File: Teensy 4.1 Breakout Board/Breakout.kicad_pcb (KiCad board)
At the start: 2 copper layers, 81.4 x 64.3 mm, 59 parts, among them J1 CAN, J10 RTD_Speaker, J11 Current Sensor Power source, J12 RTD_button, J2 12V Power, J3 APPS1, J4 APPS2, J5 Brake_Pressure_Front, J6 Brake_Pressure_Rear, J7 Nextion, J8 ESP32, J9 Brake_Light, Q1 2N7000, Q2 2N7000, U1 SN65HVD230, U3 Teensy4.1, U4 TPS62163DSG, U5 MPU6050

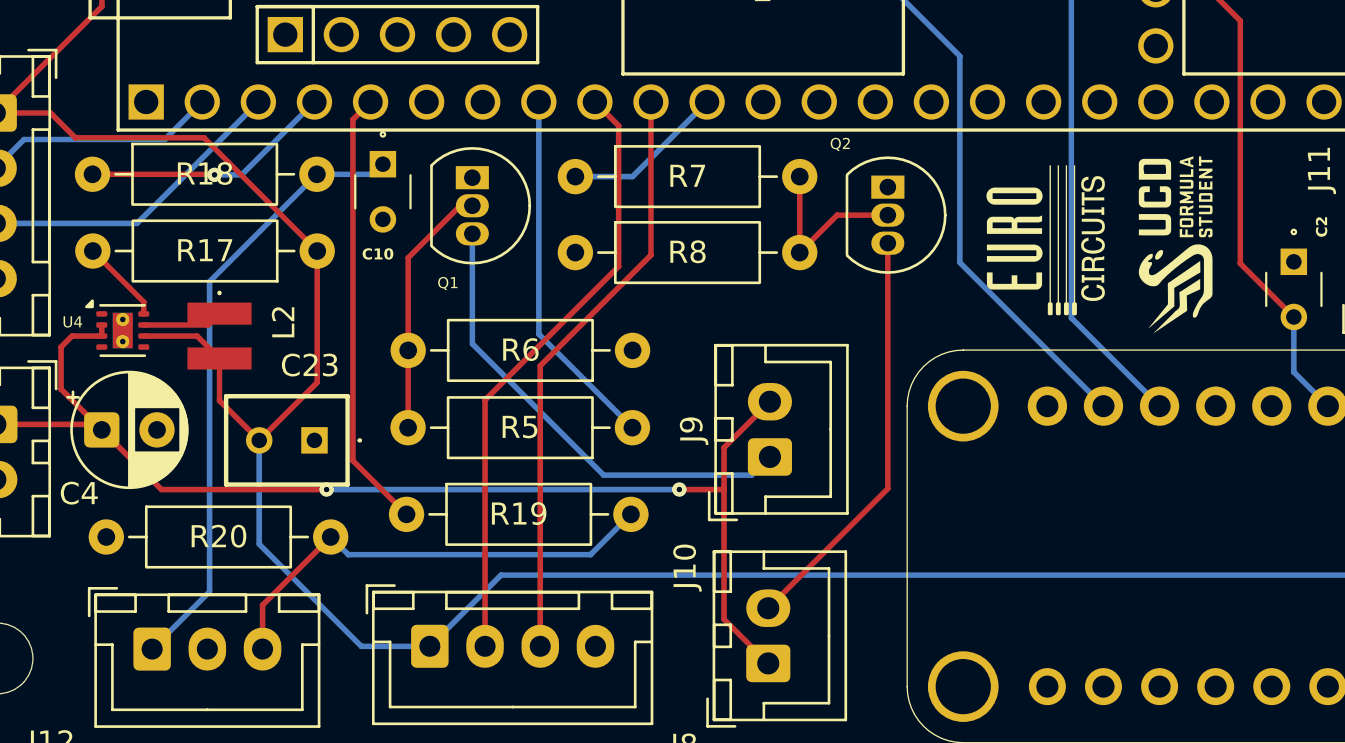
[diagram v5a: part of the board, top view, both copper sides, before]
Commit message: slave with new fuses added
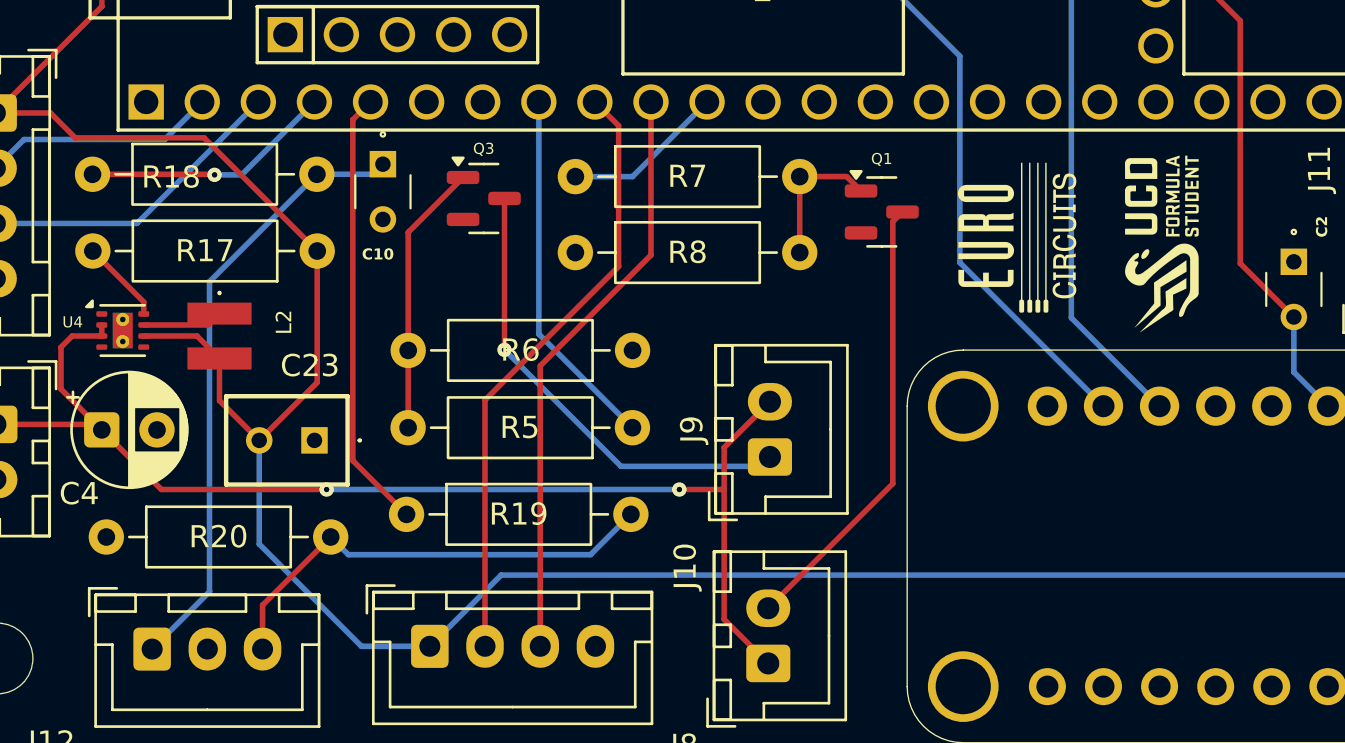
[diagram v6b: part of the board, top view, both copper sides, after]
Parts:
- removed Q2: 2N7000, Package_TO_SOT_THT:TO-92_Inline
- added Q3: 2N7002, Package_TO_SOT_SMD:SOT-23, F.Cu at (165.4, 112.8)
- Q1: value 2N7000 -> 2N7002; footprint Package_TO_SOT_THT:TO-92_Inline -> Package_TO_SOT_SMD:SOT-23
- moved Q1 18.6 mm to (183.4, 113.4), turned to 0 degrees
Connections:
- Q1 pad 1: CAN_GND -> Net-(Q1-G)
- Q1 pad 2: Net-(Q1-G) -> CAN_GND
- Q1 pad 3: Net-(J9-Pin_1) -> Net-(J10-Pin_2)
- R5 pad 2: Net-(Q1-G) -> Net-(Q3-G)
- R6 pad 2: Net-(Q1-G) -> Net-(Q3-G)
- R7 pad 2: Net-(Q2-G) -> Net-(Q1-G)
- R8 pad 2: Net-(Q2-G) -> Net-(Q1-G)
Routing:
- net Net-(Q3-G): track 0.00 -> 12.4 mm
- net Net-(Q2-G): track 8.13 -> 0.00 mm
- net Net-(Q1-G): track 11.6 -> 6.49 mm
- net Net-(J10-Pin_2): track 18.8 -> 20.5 mm
- net Net-(J9-Pin_1): track 21.3 -> 21.2 mm, vias 0 -> 1

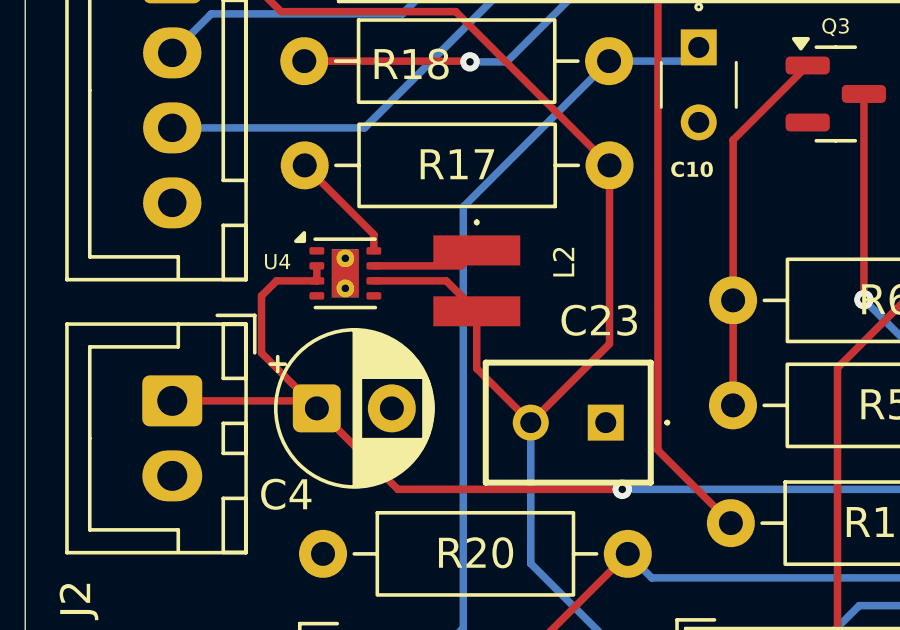
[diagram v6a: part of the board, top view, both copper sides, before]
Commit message: Slave with SMD and no other fuses
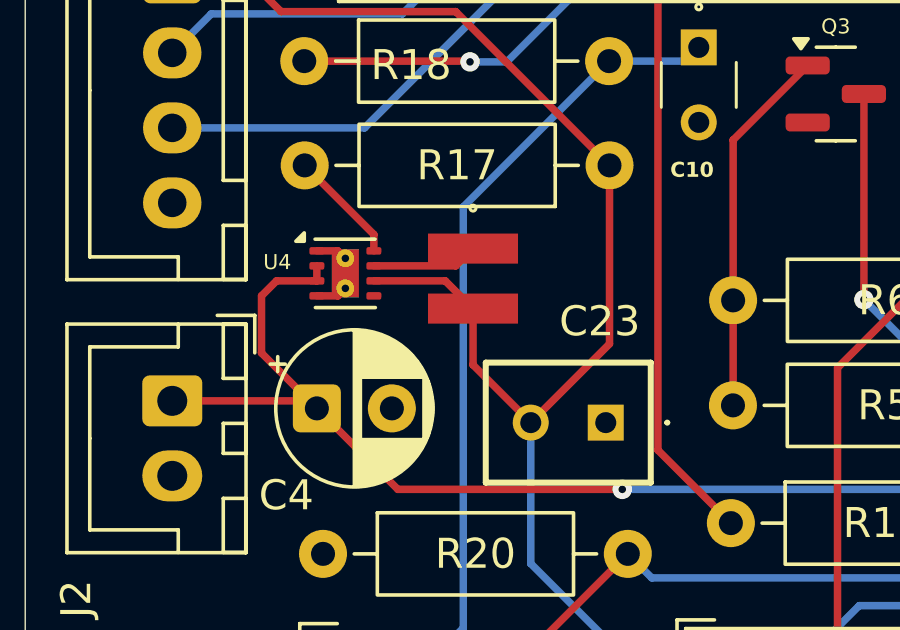
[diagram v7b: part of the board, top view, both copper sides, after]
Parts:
- removed L2: 2.2uH, XFL3012222:XFL3012222MEC
- added L1: VLS3015CX-2R2M-1, Kicad_Libraries:VLS3015, F.Cu at (153.3, 118.9)
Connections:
- U4 pad 9: unconnected-(U4-PAD-Pad9) -> CAN_GND
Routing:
- net CAN_GND: track 0.00 -> 2.11 mm
